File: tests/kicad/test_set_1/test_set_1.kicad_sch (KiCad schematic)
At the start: 1 part, among them J4 Conn_01x24_Socket

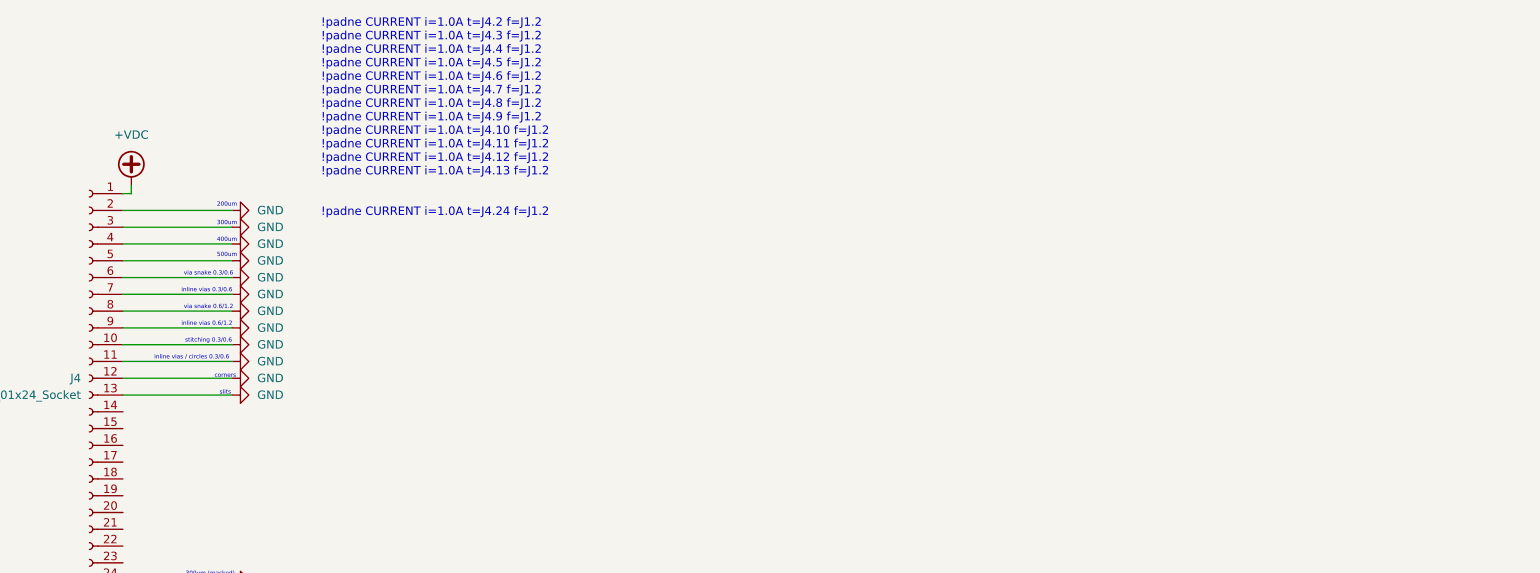
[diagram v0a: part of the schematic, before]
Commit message: test: More progress on the test_set_1 board
Add explicit test point pads to make test suite integration easier.
Also finish the "weird geometry" bunch of test cases.
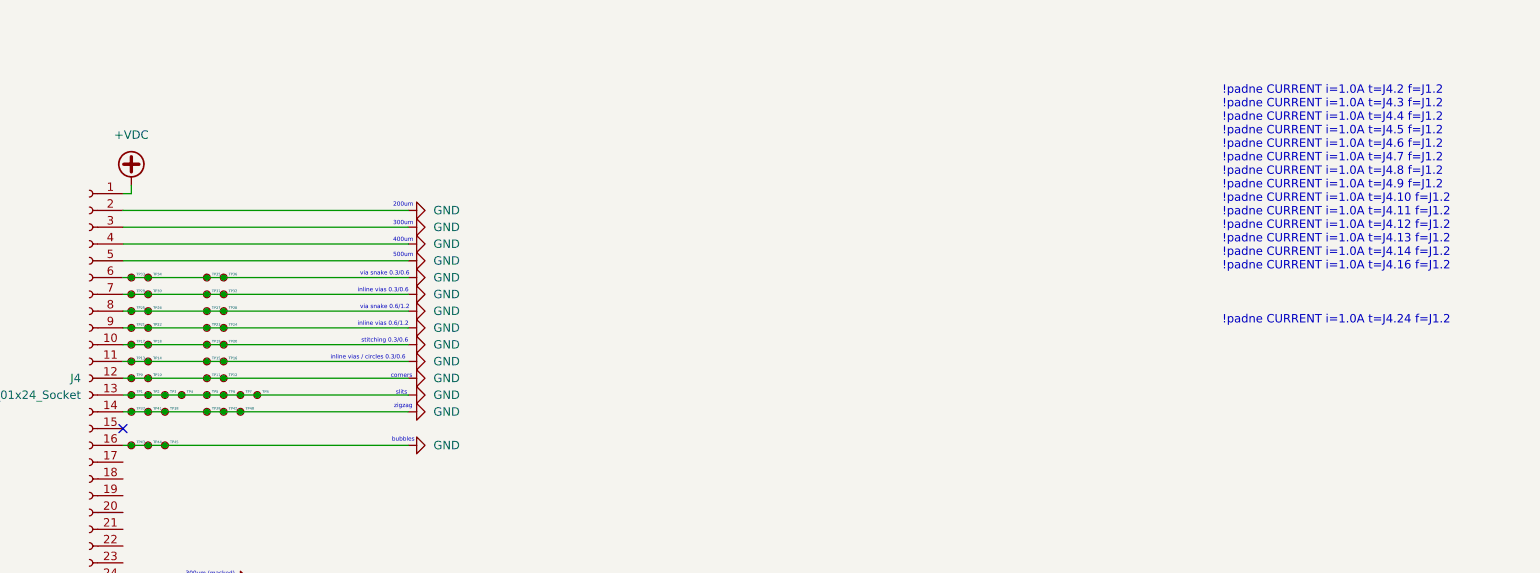
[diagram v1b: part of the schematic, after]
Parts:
- added TP1, TP10, TP11, TP12, TP13, TP14, TP15, TP16, TP17, TP18, TP19, TP2, TP20, TP21, TP22, TP23, TP24, TP25, TP26, TP27, TP28, TP29, TP3, TP30, TP31, TP32, TP33, TP34, TP35, TP36, TP37, TP38, TP39, TP4, TP40, TP41, TP42, TP43, TP44, TP45, TP5, TP6, TP7, TP8, TP9: TestPoint_Small, padne_footprints:ProbePoint, symbol Connector:TestPoint_Small
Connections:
- net GND: now also J4.14 (Pin_14), J4.16 (Pin_16), TP1.1, TP10.1, TP11.1, TP12.1, TP13.1, TP14.1, TP15.1, TP16.1, TP17.1, TP18.1, TP19.1, TP2.1, TP20.1, TP21.1, TP22.1, TP23.1, TP24.1, TP25.1, TP26.1, TP27.1, TP28.1, TP29.1, TP3.1, TP30.1, TP31.1, TP32.1, TP33.1, TP34.1, TP35.1, TP36.1, TP37.1, TP38.1, TP39.1, TP4.1, TP40.1, TP41.1, TP42.1, TP43.1, TP44.1, TP45.1, TP5.1, TP6.1, TP7.1, TP8.1, TP9.1
- no-connect marks 0 -> 1
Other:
- note added: "bubbles"
- note added: "zigzag"

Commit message: test: test_set_1 board almost finished
Gonna sleep on it a bit and then yolo order it.
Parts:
- added R1, R10, R11, R12, R13, R14, R15, R16, R17, R18, R2, R3, R4, R5, R6, R7, R8, R9: 5u, Resistor_SMD:R_1206_3216Metric, symbol Device:R_Small
- added R19, R21, R23, R25, R27, R29, R31: 5u, Resistor_SMD:R_2512_6332Metric, symbol Device:R_Small
- added R20, R22, R24, R26, R28, R30, R32, R33, R34, R35, R36, R37, R38, R39, R40, R41, R42, R43: 5u, Resistor_SMD:R_0805_2012Metric, symbol Device:R_Small
- added SYM1: Logo_Open_Hardware_Large, Symbol:OSHW-Symbol_6.7x6mm_SilkScreen, symbol Graphic:Logo_Open_Hardware_Large
- added TP46, TP47, TP48, TP49, TP50, TP51, TP52, TP53, TP54, TP55, TP56, TP57: TestPoint_Small, padne_footprints:ProbePoint, symbol Connector:TestPoint_Small
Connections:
- net GND: now also J4.23 (Pin_23), R18.2, R31.2, R34.2, R43.2, R9.2, TP46.1, TP49.1, TP52.1, TP53.1, TP55.1
- net at J4.17 (Pin_17): now also R1.1, TP47.1
- net at J4.18 (Pin_18): now also R10.1, TP48.1
- net at J4.19 (Pin_19): now also R19.1, TP51.1
- net at J4.20 (Pin_20): now also R20.1, TP50.1
- net at J4.21 (Pin_21): now also R35.1, TP54.1
- new net: R6.1, R7.1
- new net: R7.2, R8.2
- new net: R23.2, R25.1
- new net: R25.2, R27.1
- new net: R12.2, R13.1
- new net: R13.2, R14.1
- new net: R11.2, R12.1
- new net: R40.1, R41.1
- new net: R41.2, R42.2
- new net: R35.2, R36.1
- new net: R33.1, R34.1
- new net: R20.2, R22.1
- new net: R8.1, R9.1
- new net: R19.2, R21.1
- new net: R3.2, R4.1
- new net: R4.2, R5.1
- new net: R30.1, R32.1
- new net: R32.2, R33.2
- new net: R17.1, R18.1
- new net: R29.1, R31.1
- new net: R27.2, R29.2
- new net: R36.2, R37.1
- new net: R10.2, R11.1
- new net: R2.2, R3.1
- new net: R1.2, R2.1
- new net: R22.2, R24.1
- new net: R37.2, R38.1, TP56.1
- new net: R5.2, R6.2
- new net: R38.2, R39.1
- new net: R16.2, R17.2
- new net: R28.2, R30.2, TP57.1
- new net: R15.1, R16.1
- new net: R21.2, R23.1
- new net: R39.2, R40.2
- new net: R14.2, R15.2
- new net: R42.1, R43.1
- new net: R24.2, R26.1
- new net: R26.2, R28.1
- no-connect marks 1 -> 3
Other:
- note added: "!padne RESISTANCE r=0.005 a=R1.1 b=R1.2 !padne RESISTANCE r=0.005 a=R2.1 b=R2.2 !padne RESISTANCE r=0.005 a=R3.1 b=R3.2 !padne RESISTANCE r=0.005 a=R4.1 b=R4.2 !padne RESISTANCE r=0.005 a=R5.1 b=R5.2 !padne RESISTANCE r=0.005 a=R6.1 b=R6.2 !padne RESISTANCE r=0.005 a=R7.1 b=R7.2 !padne RESISTANCE r=0.005 a=R8.1 b=R8.2 !padne RESISTANCE r=0.005 a=R9.1 b=R9.2"
- note added: "!padne RESISTANCE r=0.005 a=R10.1 b=R10.2 !padne RESISTANCE r=0.005 a=R11.1 b=R11.2 !padne RESISTANCE r=0.005 a=R12.1 b=R12.2 !padne RESISTANCE r=0.005 a=R13.1 b=R13.2 !padne RESISTANCE r=0.005 a=R14.1 b=R14.2 !padne RESISTANCE r=0.005 a=R15.1 b=R15.2 !padne RESISTANCE r=0.005 a=R16.1 b=R16.2 !padne RESISTANCE r=0.005 a=R17.1 b=R17.2 !padne RESISTANCE r=0.005 a=R18.1 b=R18.2"
- note added: "!padne RESISTANCE r=0.005 a=R19.1 b=R19.2 !padne RESISTANCE r=0.005 a=R21.1 b=R21.2 !padne RESISTANCE r=0.005 a=R23.1 b=R23.2 !padne RESISTANCE r=0.005 a=R25.1 b=R25.2 !padne RESISTANCE r=0.005 a=R27.1 b=R27.2 !padne RESISTANCE r=0.005 a=R29.1 b=R29.2 !padne RESISTANCE r=0.005 a=R31.1 b=R31.2"
- note added: "!padne RESISTANCE r=0.005 a=R20.1 b=R20.2 !padne RESISTANCE r=0.005 a=R22.1 b=R22.2 !padne RESISTANCE r=0.005 a=R24.1 b=R24.2 !padne RESISTANCE r=0.005 a=R26.1 b=R26.2 !padne RESISTANCE r=0.005 a=R28.1 b=R28.2 !padne RESISTANCE r=0.005 a=R30.1 b=R30.2 !padne RESISTANCE r=0.005 a=R32.1 b=R32.2 !padne RESISTANCE r=0.005 a=R33.1 b=R33.2 !padne RESISTANCE r=0.005 a=R34.1 b=R34.2"
- note added: "200um (masked)"
- note added: "400um (masked)"
- note removed: "300um (masked)"

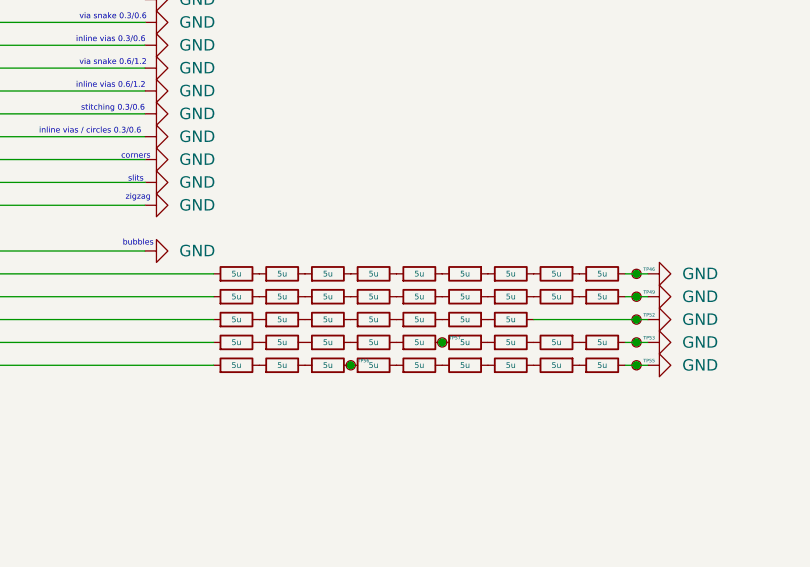
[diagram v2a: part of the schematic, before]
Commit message: test: test_set_1 finishing touches (silkscreen and more test pads)
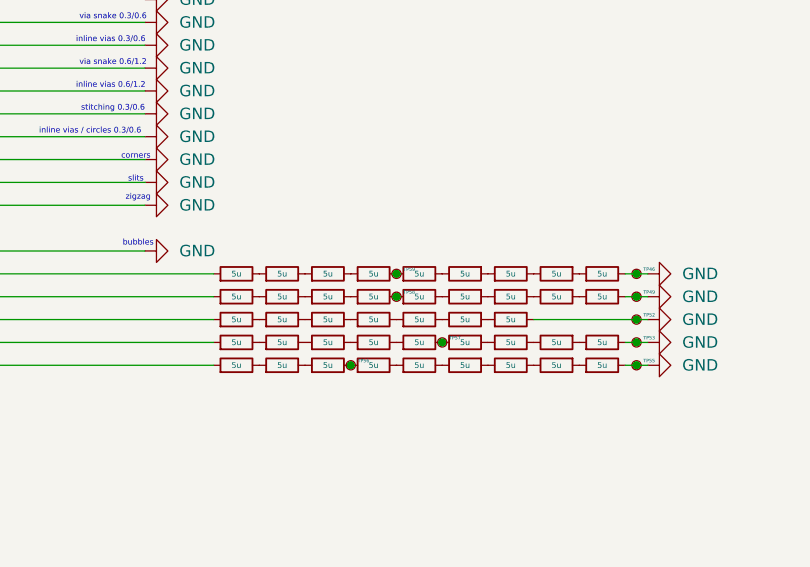
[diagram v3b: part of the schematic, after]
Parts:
- added TP58, TP59: TestPoint_Small, padne_footprints:ProbePoint, symbol Connector:TestPoint_Small
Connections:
- net at R13.2, R14.1: now also TP58.1
- net at R4.2, R5.1: now also TP59.1
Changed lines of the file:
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@@
 	)
 	(junction
+		(at 142.24 71.12)
+		(diameter 0)
+		(color 0 0 0 0)
+	)
+	(junction
 		(at 74.93 60.96)
 		(diameter 0)
@@
 	)
 	(junction
+		(at 142.24 73.66)
+		(diameter 0)
+		(color 0 0 0 0)
+	)
+	(junction
 		(at 137.16 81.28)
 		(diameter 0)
@@
 		(at 33.02 180.34 0)
 		(unit 1)
-		(exclude_from_sim no)
+		(exclude_from_sim yes)
 		(in_bom yes)
 		(on_board yes)
@@
 			)
 		)
-		(property "Sim.Enable" "0"
-			(at 33.02 180.34 0)
-			(effects
-				(font
-					(size 1.27 1.27)
-				)
-				(hide yes)
-			)
-		)
 		(instances
 			(project ""
@@
 	(symbol
 		(lib_id "Connector:TestPoint_Small")
+		(at 142.24 71.12 0)
+		(unit 1)
+		(exclude_from_sim no)
+		(in_bom yes)
+		(on_board yes)
+		(dnp no)
+		(property "Reference" "TP59"
+			(at 143.002 70.612 0)
+			(effects
+				(font
+					(size 0.381 0.381)
+				)
+				(justify left)
+			)
+		)
+		(property "Value" "TestPoint_Small"
+			(at 143.51 72.3899 0)
+			(effects
+				(font
+					(size 1.27 1.27)
+				)
+				(justify left)
+				(hide yes)
+			)
+		)
+		(property "Footprint" "padne_footprints:ProbePoint"
+			(at 147.32 71.12 0)
+			(effects
+				(font
+					(size 1.27 1.27)
+				)
+				(hide yes)
+			)
+		)
+		(property "Datasheet" "~"
+			(at 147.32 71.12 0)
+			(effects
+				(font
+					(size 1.27 1.27)
+				)
+				(hide yes)
+			)
+		)
+		(property "Description" "test point"
+			(at 142.24 71.12 0)
+			(effects
+				(font
+					(size 1.27 1.27)
+				)
+				(hide yes)
+			)
+		)
+		(pin "1"
+		)
+		(instances
+			(project "test_set_1"
+				(path "/1de6d912-4613-4162-994c-48d82d6366f0"
+					(reference "TP59")
+					(unit 1)
+				)
+			)
+		)
+	)
+	(symbol
+		(lib_id "Connector:TestPoint_Small")
 		(at 74.93 43.18 0)
 		(unit 1)
@@
 					(unit 1)
 				)
+			)
+		)
+	)
+	(symbol
+		(lib_id "Connector:TestPoint_Small")
+		(at 142.24 73.66 0)
+		(unit 1)
+		(exclude_from_sim no)
+		(in_bom yes)
+		(on_board yes)
+		(dnp no)
+		(property "Reference" "TP58"
+			(at 143.002 73.152 0)
+			(effects
+				(font
+					(size 0.381 0.381)
+				)
+				(justify left)
+			)
+		)
+		(property "Value" "TestPoint_Small"
+			(at 143.51 74.9299 0)
+			(effects
+				(font
+					(size 1.27 1.27)
+				)
+				(justify left)
+				(hide yes)
+			)
+		)
+		(property "Footprint" "padne_footprints:ProbePoint"
+			(at 147.32 73.66 0)
+			(effects
+				(font
+					(size 1.27 1.27)
+				)
+				(hide yes)
+			)
+		)
+		(property "Datasheet" "~"
+			(at 147.32 73.66 0)
+			(effects
+				(font
+					(size 1.27 1.27)
+				)
+				(hide yes)
+			)
+		)
+		(property "Description" "test point"
+			(at 142.24 73.66 0)
+			(effects
+				(font
+					(size 1.27 1.27)
+				)
+				(hide yes)
+			)
+		)
+		(pin "1"
+		)
+		(instances
+			(project "test_set_1"
+				(path "/1de6d912-4613-4162-994c-48d82d6366f0"
+					(reference "TP58")
+					(unit 1)
+				)

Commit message: test: Add probe points to test_set_1
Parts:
- added TP60, TP61, TP62, TP63, TP64, TP65, TP66, TP67: TestPoint_Small, padne_footprints:ProbePoint, symbol Connector:TestPoint_Small
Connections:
- net GND: now also TP60.1, TP61.1, TP62.1, TP63.1, TP64.1, TP65.1, TP66.1, TP67.1
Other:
- note added: "!padne PROBE p=TP1.1,TP10.1,TP11.1,TP12.1,TP13.1,TP14.1,TP15.1,TP16.1,TP17.1,TP18.1,TP19.1,TP2.1,TP20.1,TP21.1,TP22.1,TP23.1,TP24.1,TP25.1,TP26.1,TP27.1,TP28.1,TP29.1,TP3.1,TP30.1,TP31.1,TP32.1,TP33.1,TP34.1,TP35.1,TP36.1,TP37.1,TP38.1,TP39.1,TP4.1,TP40.1,TP41.1,TP42.1,TP43.1,TP44.1,TP45.1,TP46.1,TP47.1,TP48.1,TP49.1,TP5.1,TP50.1,TP51.1,TP52.1,TP53.1,TP54.1,TP55.1,TP56.1,TP57.1,TP58.1,TP59.1,TP6.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"
